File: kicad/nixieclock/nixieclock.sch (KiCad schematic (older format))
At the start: 17 parts

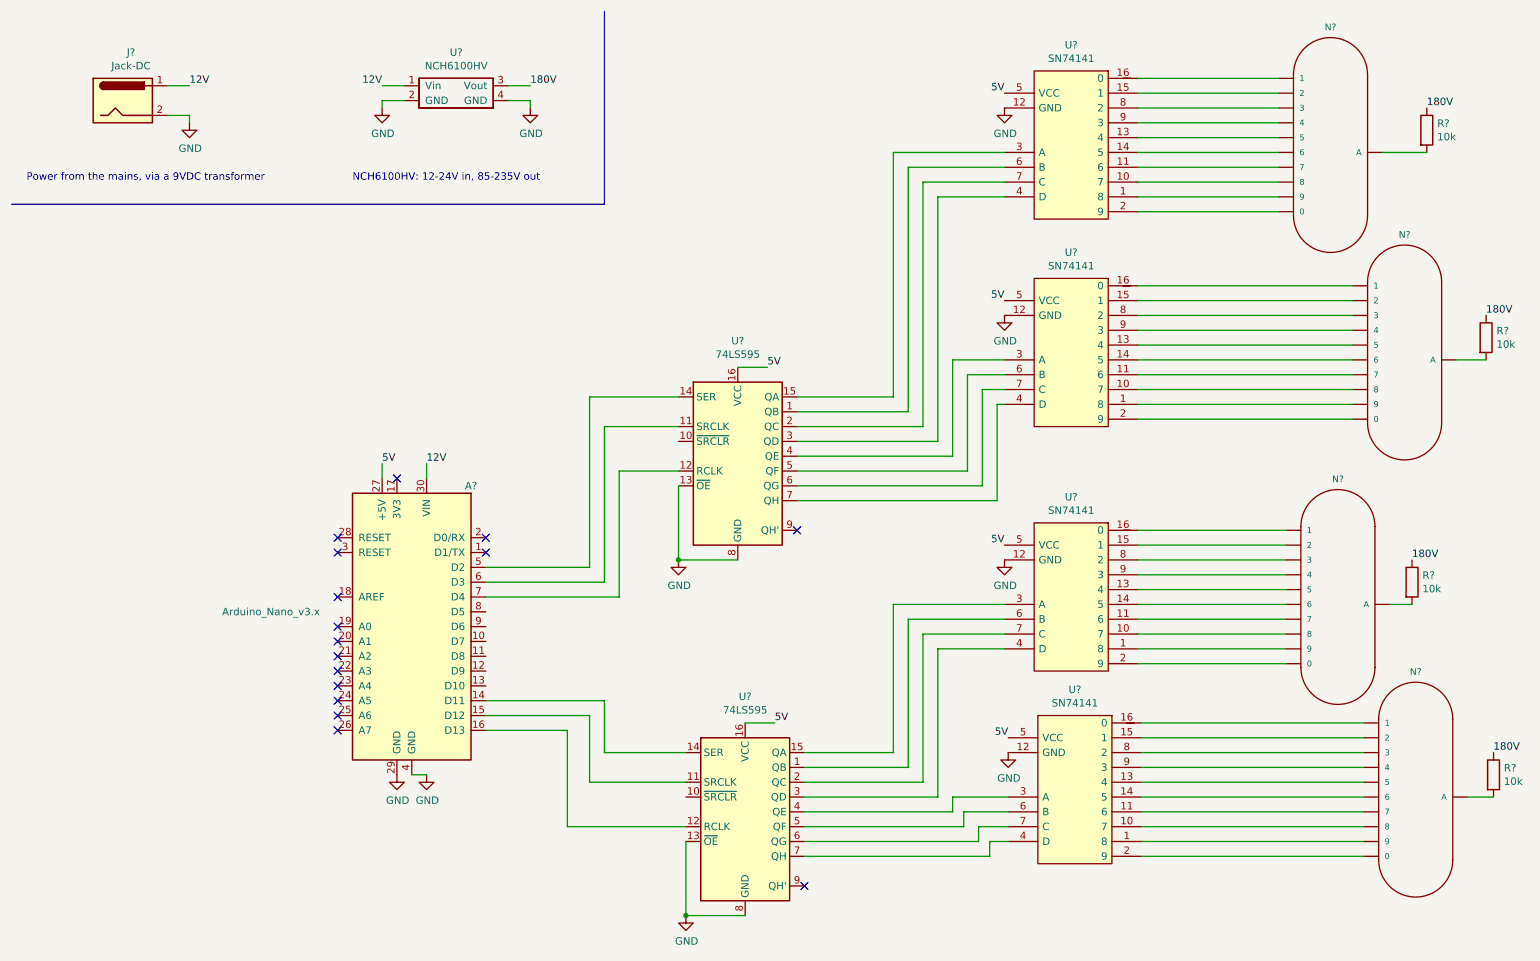
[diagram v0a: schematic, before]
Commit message: Fix: annotate components
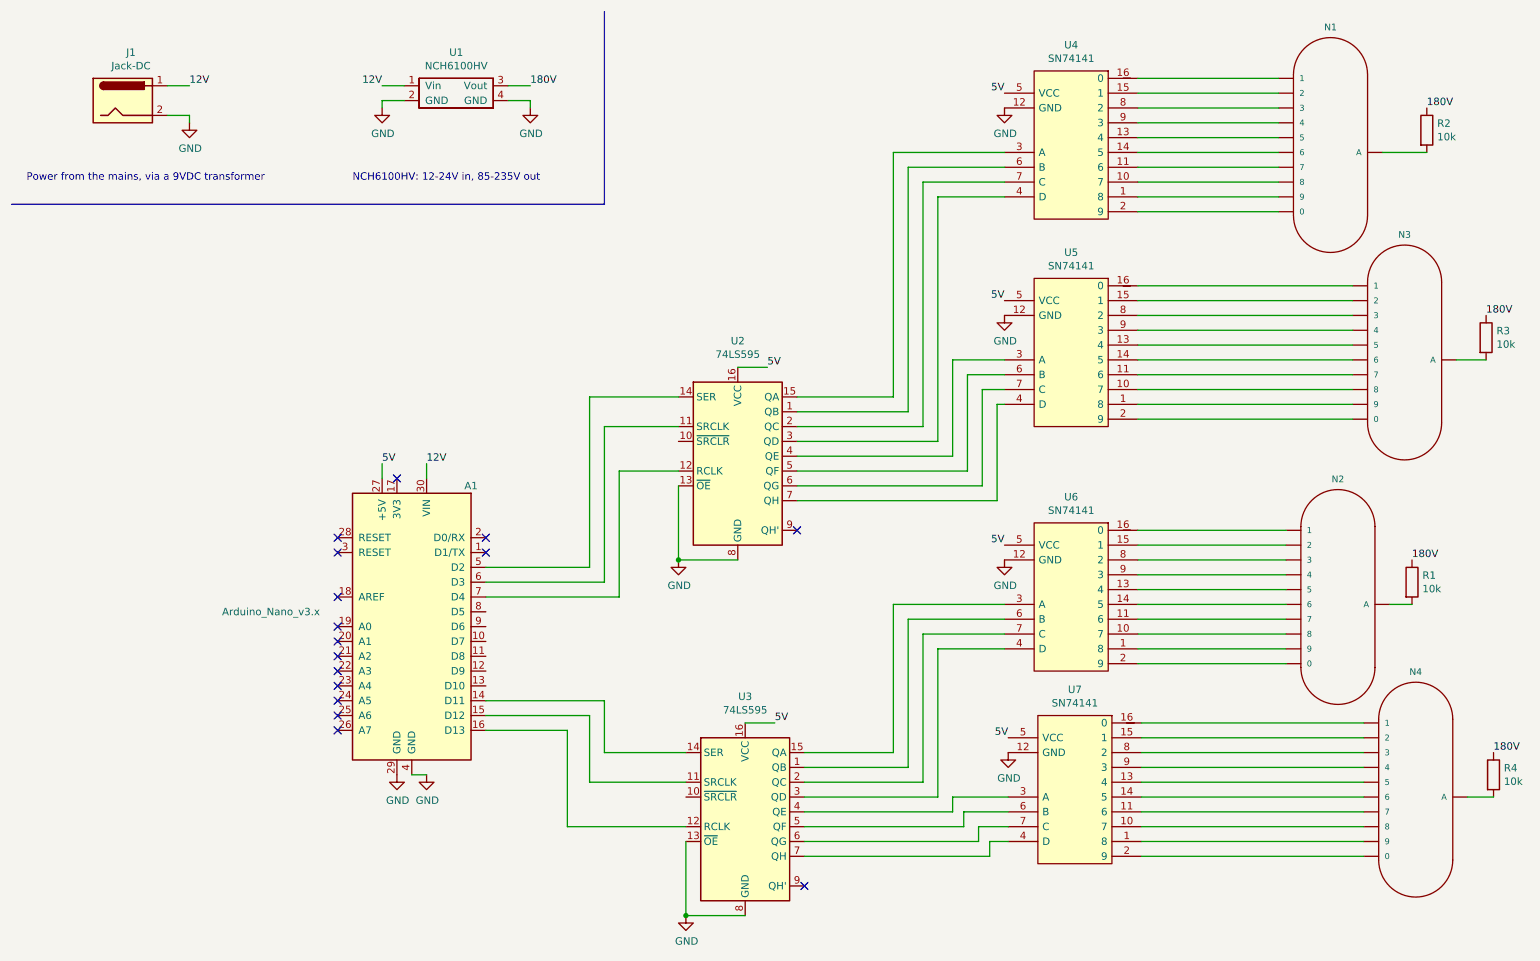
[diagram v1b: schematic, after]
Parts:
- gave numbers to parts that had none: 17
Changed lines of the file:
@@
 EESchema Schematic File Version 4
+LIBS:nixieclock-cache
 EELAYER 26 0
 EELAYER END
@@
 $EndDescr
 $Comp
-L Connector:Jack-DC J?
+L Connector:Jack-DC J1
 U 1 1 5C2359A9
 P 1300 1150
-F 0 "J?" H 1355 1475 50  0000 C CNN
+F 0 "J1" H 1355 1475 50  0000 C CNN
 F 1 "Jack-DC" H 1355 1384 50  0000 C CNN
 F 2 "" H 1350 1110 50  0001 C CNN
@@
 $EndComp
 $Comp
-L power:GND #PWR?
+L power:GND #PWR01
 U 1 1 5C235ABA
 P 1750 1300
-F 0 "#PWR?" H 1750 1050 50  0001 C CNN
+F 0 "#PWR01" H 1750 1050 50  0001 C CNN
 F 1 "GND" H 1755 1127 50  0000 C CNN
 F 2 "" H 1750 1300 50  0001 C CNN
@@
 12V
 $Comp
-L Converter_DCDC:NCH6100HV U?
+L Converter_DCDC:NCH6100HV U1
 U 1 1 5C2366AA
 P 3550 1100
-F 0 "U?" H 3550 1375 50  0000 C CNN
+F 0 "U1" H 3550 1375 50  0000 C CNN
 F 1 "NCH6100HV" H 3550 1284 50  0000 C CNN
 F 2 "" H 3550 1100 50  0001 C CNN
@@
 	3050 1150 3050 1200
 $Comp
-L power:GND #PWR?
+L power:GND #PWR02
 U 1 1 5C2367D1
 P 3050 1200
-F 0 "#PWR?" H 3050 950 50  0001 C CNN
+F 0 "#PWR02" H 3050 950 50  0001 C CNN
 F 1 "GND" H 3055 1027 50  0000 C CNN
 F 2 "" H 3050 1200 50  0001 C CNN
@@
 	4050 1150 4050 1200
 $Comp
-L power:GND #PWR?
+L power:GND #PWR05
 U 1 1 5C236925
 P 4050 1200
-F 0 "#PWR?" H 4050 950 50  0001 C CNN
+F 0 "#PWR05" H 4050 950 50  0001 C CNN
 F 1 "GND" H 4055 1027 50  0000 C CNN
 F 2 "" H 4050 1200 50  0001 C CNN
@@
 180V
 $Comp
-L MCU_Module:Arduino_Nano_v3.x A?
+L MCU_Module:Arduino_Nano_v3.x A1
 U 1 1 5C236ACE
 P 3250 4700
-F 0 "A?" H 2850 5650 50  0000 C CNN
+F 0 "A1" H 2850 5650 50  0000 C CNN
 F 1 "Arduino_Nano_v3.x" H 4200 4800 50  0000 C CNN
 F 2 "Module:Arduino_Nano" H 3400 3750 50  0001 L CNN
@@
 NoConn ~ 3750 4200
 $Comp
-L power:GND #PWR?
+L power:GND #PWR03
 U 1 1 5C237A67
 P 3150 5700
-F 0 "#PWR?" H 3150 5450 50  0001 C CNN
+F 0 "#PWR03" H 3150 5450 50  0001 C CNN
 F 1 "GND" H 3155 5527 50  0000 C CNN
 F 2 "" H 3150 5700 50  0001 C CNN
@@
 $EndComp
 $Comp
-L power:GND #PWR?
+L power:GND #PWR04
 U 1 1 5C237B76
 P 3350 5700
-F 0 "#PWR?" H 3350 5450 50  0001 C CNN
+F 0 "#PWR04" H 3350 5450 50  0001 C CNN
 F 1 "GND" H 3355 5527 50  0000 C CNN
 F 2 "" H 3350 5700 50  0001 C CNN
@@
 12V
 $Comp
-L 74xx:74LS595 U?
+L 74xx:74LS595 U2
 U 1 1 5C2380EA
 P 5450 3550
-F 0 "U?" H 5450 4328 50  0000 C CNN
+F 0 "U2" H 5450 4328 50  0000 C CNN
 F 1 "74LS595" H 5450 4237 50  0000 C CNN
 F 2 "" H 5450 3550 50  0001 C CNN
@@
 $EndComp
 $Comp
-L 74xx:74LS595 U?
+L 74xx:74LS595 U3
 U 1 1 5C238148
 P 5500 5950
-F 0 "U?" H 5500 6728 50  0000 C CNN
+F 0 "U3" H 5500 6728 50  0000 C CNN
 F 1 "74LS595" H 5500 6637 50  0000 C CNN
 F 2 "" H 5500 5950 50  0001 C CNN
@@
 $EndComp
 $Comp
-L SN74141:SN74141 U?
+L SN74141:SN74141 U4
 U 1 1 5C239166
 P 7700 1450
-F 0 "U?" H 7700 2125 50  0000 C CNN
+F 0 "U4" H 7700 2125 50  0000 C CNN
 F 1 "SN74141" H 7700 2034 50  0000 C CNN
 F 2 "DIP787W53P279L2176H508Q16N" H 8750 1550 50  0001 L CNN
@@
 $EndComp
 $Comp
-L SN74141:SN74141 U?
+L SN74141:SN74141 U5
 U 1 1 5C23923C
 P 7700 2850
-F 0 "U?" H 7700 3525 50  0000 C CNN
+F 0 "U5" H 7700 3525 50  0000 C CNN
 F 1 "SN74141" H 7700 3434 50  0000 C CNN
 F 2 "DIP787W53P279L2176H508Q16N" H 8750 2950 50  0001 L CNN
@@
 $EndComp
 $Comp
-L SN74141:SN74141 U?
+L SN74141:SN74141 U6
 U 1 1 5C239314
 P 7700 4500
-F 0 "U?" H 7700 5175 50  0000 C CNN
+F 0 "U6" H 7700 5175 50  0000 C CNN
 F 1 "SN74141" H 7700 5084 50  0000 C CNN
 F 2 "DIP787W53P279L2176H508Q16N" H 8750 4600 50  0001 L CNN
@@
 $EndComp
 $Comp
-L SN74141:SN74141 U?
+L SN74141:SN74141 U7
 U 1 1 5C23935A
 P 7725 5800
-F 0 "U?" H 7725 6475 50  0000 C CNN
+F 0 "U7" H 7725 6475 50  0000 C CNN
 F 1 "SN74141" H 7725 6384 50  0000 C CNN
 F 2 "DIP787W53P279L2176H508Q16N" H 8775 5900 50  0001 L CNN
@@
 	4300 6050 5100 6050
 $Comp
-L power:GND #PWR?
+L power:GND #PWR06
 U 1 1 5C23AF0A
 P 5050 4250
-F 0 "#PWR?" H 5050 4000 50  0001 C CNN
+F 0 "#PWR06" H 5050 4000 50  0001 C CNN
 F 1 "GND" H 5055 4077 50  0000 C CNN
 F 2 "" H 5050 4250 50  0001 C CNN
@@
 	5100 6650 5500 6650
 $Comp
-L power:GND #PWR?
+L power:GND #PWR07
 U 1 1 5C23BD89
 P 5100 6650
-F 0 "#PWR?" H 5100 6400 50  0001 C CNN
+F 0 "#PWR07" H 5100 6400 50  0001 C CNN
 F 1 "GND" H 5105 6477 50  0000 C CNN
 F 2 "" H 5100 6650 50  0001 C CNN
@@
 5V
 $Comp
-L power:GND #PWR?
+L power:GND #PWR08
 U 1 1 5C24E1DE
 P 7250 1200
-F 0 "#PWR?" H 7250 950 50  0001 C CNN
+F 0 "#PWR08" H 7250 950 50  0001 C CNN
 F 1 "GND" H 7255 1027 50  0000 C CNN
 F 2 "" H 7250 1200 50  0001 C CNN
@@
 $EndComp
 $Comp
-L power:GND #PWR?
+L power:GND #PWR09
 U 1 1 5C24E22F
 P 7250 2600
-F 0 "#PWR?" H 7250 2350 50  0001 C CNN
+F 0 "#PWR09" H 7250 2350 50  0001 C CNN
 F 1 "GND" H 7255 2427 50  0000 C CNN
 F 2 "" H 7250 2600 50  0001 C CNN
@@
 $EndComp
 $Comp
-L power:GND #PWR?
+L power:GND #PWR010
 U 1 1 5C24E2A6
 P 7250 4250
-F 0 "#PWR?" H 7250 4000 50  0001 C CNN
+F 0 "#PWR010" H 7250 4000 50  0001 C CNN
 F 1 "GND" H 7255 4077 50  0000 C CNN
 F 2 "" H 7250 4250 50  0001 C CNN
@@
 $EndComp
 $Comp
-L power:GND #PWR?
+L power:GND #PWR011
 U 1 1 5C24E314
 P 7275 5550
-F 0 "#PWR?" H 7275 5300 50  0001 C CNN
+F 0 "#PWR011" H 7275 5300 50  0001 C CNN
 F 1 "GND" H 7280 5377 50  0000 C CNN
 F 2 "" H 7275 5550 50  0001 C CNN
@@
 5V
 $Comp
-L nixie:IN-1 N?
+L nixie:IN-1 N1
 U 1 1 5C251795
 P 9500 1500
-F 0 "N?" H 9450 2345 45  0000 C CNN
+F 0 "N1" H 9450 2345 45  0000 C CNN
 F 1 "IN-1" H 9500 1500 45  0001 L BNN
 F 2 "nixies-us_IN-1" H 9530 1650 20  0001 C CNN
@@
 	8150 1900 9100 1900
 $Comp
-L nixie:IN-1 N?
+L nixie:IN-1 N3
 U 1 1 5C261ED1
 P 10000 2900
-F 0 "N?" H 9950 3745 45  0000 C CNN
+F 0 "N3" H 9950 3745 45  0000 C CNN
 F 1 "IN-1" H 10000 2900 45  0001 L BNN
 F 2 "nixies-us_IN-1" H 10030 3050 20  0001 C CNN
@@
 	8150 3300 9600 3300
 $Comp
-L nixie:IN-1 N?
+L nixie:IN-1 N2
 U 1 1 5C277054
 P 9550 4550
-F 0 "N?" H 9500 5395 45  0000 C CNN
+F 0 "N2" H 9500 5395 45  0000 C CNN
 F 1 "IN-1" H 9550 4550 45  0001 L BNN
 F 2 "nixies-us_IN-1" H 9580 4700 20  0001 C CNN
@@
 	9150 4950 8150 4950
 $Comp
-L nixie:IN-1 N?
+L nixie:IN-1 N4
 U 1 1 5C294310
 P 10075 5850
-F 0 "N?" H 10025 6695 45  0000 C CNN
+F 0 "N4" H 10025 6695 45  0000 C CNN
 F 1 "IN-1" H 10075 5850 45  0001 L BNN
 F 2 "nixies-us_IN-1" H 10105 6000 20  0001 C CNN
@@
 	8175 6250 9675 6250
 $Comp
-L Device:R R?
+L Device:R R2
 U 1 1 5C2C91FC
 P 10100 1350
-F 0 "R?" H 10170 1396 50  0000 L CNN
+F 0 "R2" H 10170 1396 50  0000 L CNN
 F 1 "10k" H 10170 1305 50  0000 L CNN
 F 2 "" V 10030 1350 50  0001 C CNN
@@
 180V
 $Comp
-L Device:R R?
+L Device:R R3
 U 1 1 5C2D1A2D
 P 10500 2750
-F 0 "R?" H 10570 2796 50  0000 L CNN
+F 0 "R3" H 10570 2796 50  0000 L CNN
 F 1 "10k" H 10570 2705 50  0000 L CNN
 F 2 "" V 10430 2750 50  0001 C CNN
@@
 $EndComp
 $Comp
-L Device:R R?
+L Device:R R1
 U 1 1 5C2D1AAE
 P 10000 4400
-F 0 "R?" H 10070 4446 50  0000 L CNN
+F 0 "R1" H 10070 4446 50  0000 L CNN
 F 1 "10k" H 10070 4355 50  0000 L CNN
 F 2 "" V 9930 4400 50  0001 C CNN
@@
 $EndComp
 $Comp
-L Device:R R?
+L Device:R R4
 U 1 1 5C2D1CC8
 P 10550 5700
-F 0 "R?" H 10620 5746 50  0000 L CNN
+F 0 "R4" H 10620 5746 50  0000 L CNN
 F 1 "10k" H 10620 5655 50  0000 L CNN
 F 2 "" V 10480 5700 50  0001 C CNN
